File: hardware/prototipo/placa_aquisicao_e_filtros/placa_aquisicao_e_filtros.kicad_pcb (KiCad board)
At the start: 2 copper layers, 20 parts, among them J1 Conn_01x04, J2 Conn_02x04_Odd_Even, J3 Conn_01x02, U1 Opamp_Quad_Generic, U2 AD620

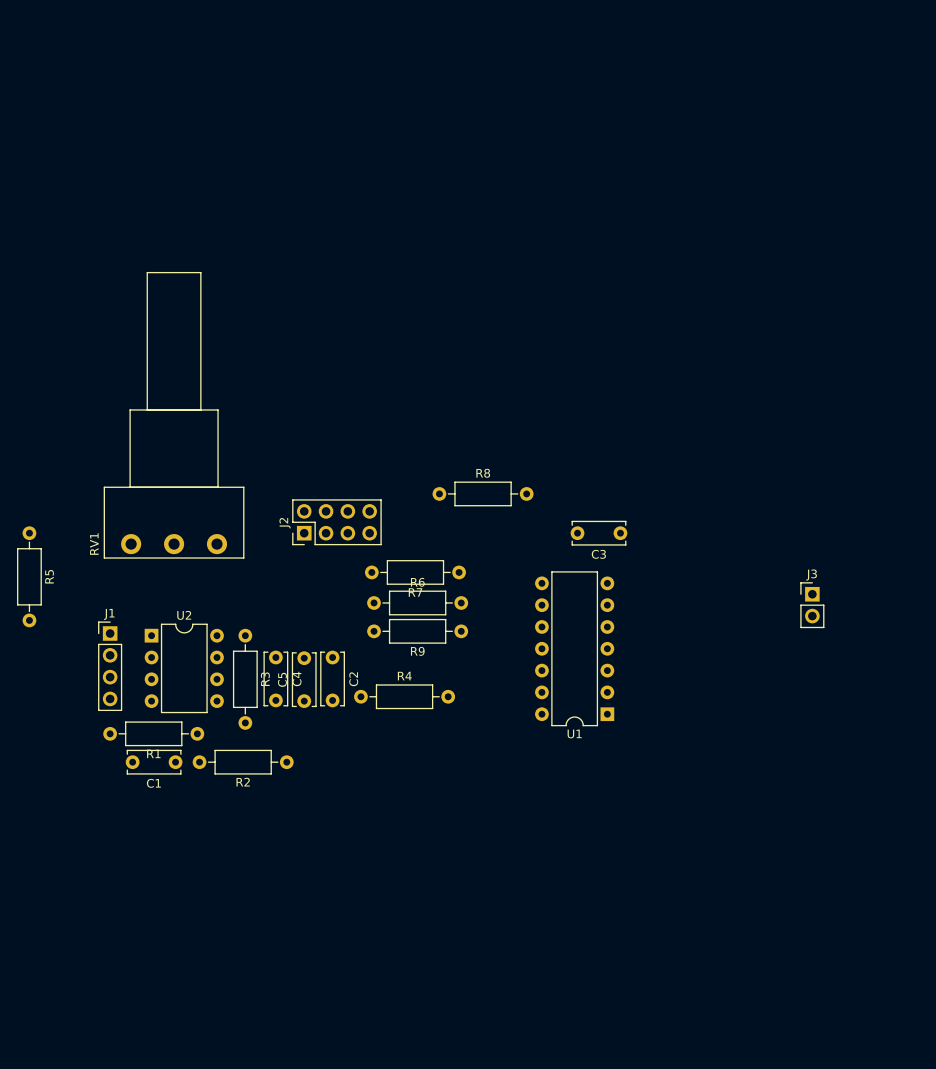
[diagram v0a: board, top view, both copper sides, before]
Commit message: Acquisition PCB prototype in development.
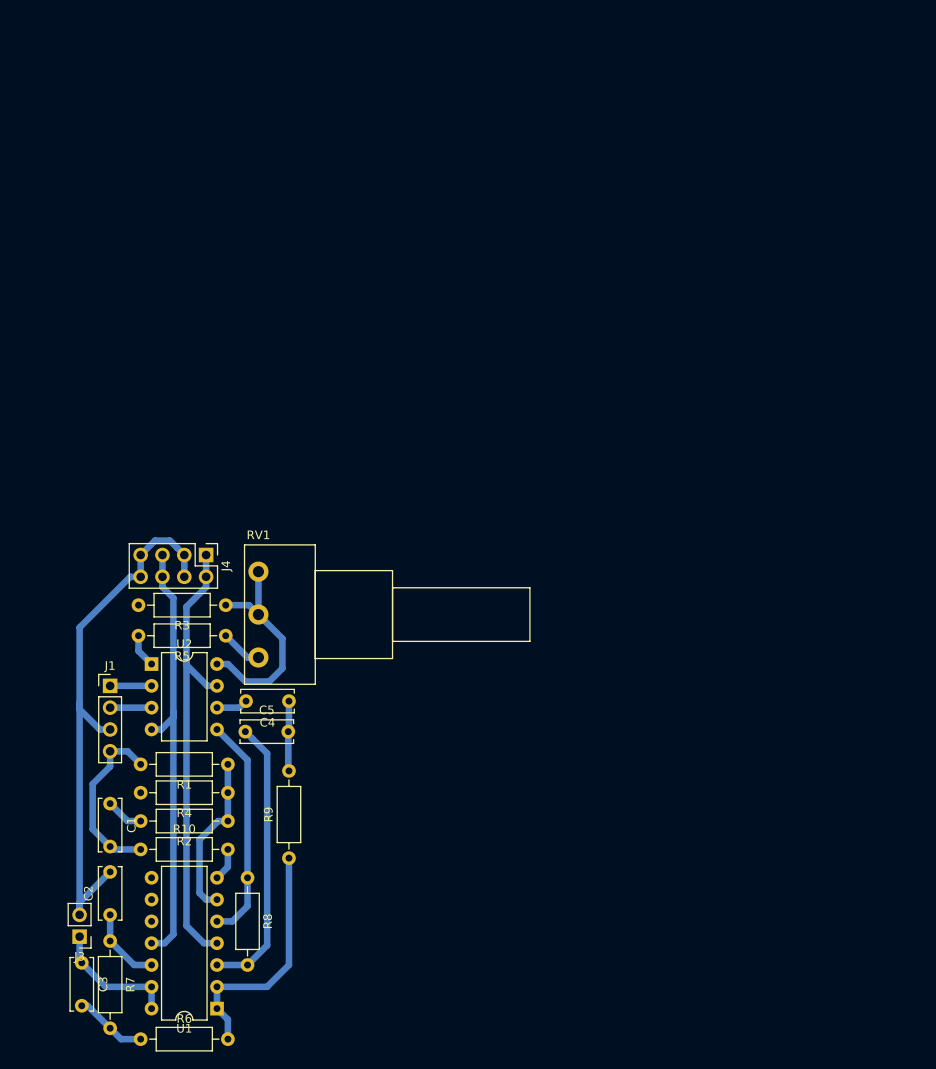
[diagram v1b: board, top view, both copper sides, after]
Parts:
- removed J2: Conn_02x04_Odd_Even, Connector_PinHeader_2.54mm:PinHeader_2x04_P2.54mm_Vertical
- added J4: Conn_02x04_Counter_Clockwise, Connector_PinHeader_2.54mm:PinHeader_2x04_P2.54mm_Vertical, F.Cu at (104.6, 83.6)
- added R10: 0R, Resistor_THT:R_Axial_DIN0207_L6.3mm_D2.5mm_P10.16mm_Horizontal, F.Cu at (97.0, 117.9)
- moved J3 94.2 mm to (89.9, 128.0), turned to 180 degrees
- moved C3 80.2 mm to (90.2, 131.1), turned to 270 degrees
- moved R7 59.1 mm to (93.5, 128.5), turned to 270 degrees
- moved R6 57.6 mm to (97.0, 140.0)
- moved U1 56.9 mm to (105.9, 136.4)
- moved R8 50.0 mm to (109.5, 121.2), turned to 270 degrees
- moved C2 39.6 mm to (93.5, 125.5), turned to 90 degrees
- moved R9 33.2 mm to (114.3, 118.9), turned to 90 degrees
- moved R5 25.8 mm to (106.9, 93.0), turned to 180 degrees
- moved R4 19.1 mm to (107.2, 111.3), turned to 180 degrees
- moved RV1 14.1 mm to (110.7, 95.5), turned to 0 degrees
- moved R2 9.70 mm to (107.2, 114.6)
- moved C1 9.02 mm to (93.5, 112.5), turned to 270 degrees
- moved C5 7.73 mm to (109.2, 104.1), turned to 0 degrees
- moved J1 6.10 mm to (93.5, 98.8)
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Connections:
- RV1 pad 1: Net-(R3-Pad1) -> Net-(R5-Pad1)
- RV1 pad 2: Net-(R5-Pad1) -> Net-(R3-Pad1)
- RV1 pad 3: Net-(R5-Pad1) -> Net-(R3-Pad1)
- U1 pad 1: ref_electrode -> out2
- U1 pad 10: Net-(C5-Pad1) -> (no net)
- U1 pad 11: (no net) -> -9V
- U1 pad 2: Net-(R1-Pad1) -> out2
- U1 pad 3: GNDA -> Net-(C5-Pad1)
- U1 pad 4: (no net) -> +9V
- U1 pad 5: Net-(C2-Pad1) -> GNDA
- U1 pad 6: out3 -> Net-(R1-Pad1)
- U1 pad 7: out3 -> Net-(R10-Pad2)
- U1 pad 8: out2 -> (no net)
- U1 pad 9: out2 -> (no net)
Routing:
- net GNDA: track 0.00 -> 92.6 mm
- net +9V: track 0.00 -> 53.7 mm
- net -9V: track 0.00 -> 51.4 mm
- net Net-(C5-Pad1): track 0.00 -> 32.7 mm
- net out2: track 0.00 -> 28.5 mm
- net Net-(R3-Pad1): track 0.00 -> 25.8 mm
- net ref_electrode: track 0.00 -> 20.7 mm
- net Net-(R1-Pad1): track 0.00 -> 19.4 mm
- net out3: track 0.00 -> 15.0 mm
- net Net-(C2-Pad1): track 0.00 -> 9.03 mm
- net Net-(C3-Pad2): track 0.00 -> 8.47 mm
- net Net-(C4-Pad1): track 0.00 -> 8.19 mm
- net Net-(R5-Pad1): track 0.00 -> 4.86 mm
- net right_electrode: track 0.00 -> 4.83 mm
- net left_electrode: track 0.00 -> 4.83 mm
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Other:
- net class Default: clearance 0.2 -> 0.45; trace_width 0.25 -> 0.762
- rule trace_clearance: 0.2 -> 0.45

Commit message: Acquisition prototype board finalized.
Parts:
- removed R10: 0R, Resistor_THT:R_Axial_DIN0207_L6.3mm_D2.5mm_P10.16mm_Horizontal
- added C6: 47u, Capacitors_THT:C_Disc_D6.0mm_W2.5mm_P5.00mm, F.Cu at (155.4, 107.8)
- added R11: 130k, Resistors_THT:R_Axial_DIN0207_L6.3mm_D2.5mm_P10.16mm_Horizontal, F.Cu at (153.8, 78.5)
- added R12: 18k, Resistors_THT:R_Axial_DIN0207_L6.3mm_D2.5mm_P10.16mm_Horizontal, F.Cu at (155.2, 122.0)
- R8: value 91k -> 33k
- R9: value 47k -> 150k
- moved R8 55.6 mm to (155.4, 89.9)
- moved C5 52.0 mm to (160.5, 95.5), turned to 90 degrees
- moved R9 50.4 mm to (160.4, 98.4), turned to 270 degrees
- moved J4 50.2 mm to (149.9, 61.7)
- moved R3 50.2 mm to (152.1, 67.6)
- moved RV1 50.2 mm to (156.0, 73.7)
- moved U2 50.2 mm to (143.5, 74.4)
- moved R5 50.2 mm to (152.1, 71.1)
- moved R1 49.3 mm to (152.4, 88.4)
- moved C4 48.6 mm to (159.1, 81.9)
- moved C1 48.2 mm to (138.7, 95.8)
- moved C2 48.2 mm to (138.7, 108.7)
- moved C3 48.2 mm to (135.4, 114.3)
- moved R2 48.2 mm to (152.4, 97.8)
- moved R4 48.2 mm to (152.4, 94.5)
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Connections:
- J1 pad 1: right_electrode -> left_electrode
- J1 pad 2: left_electrode -> right_electrode
- R8 pad 2: Net-(C5-Pad1) -> Net-(C4-Pad1)
- R9 pad 1: out2 -> Net-(C5-Pad1)
- R9 pad 2: Net-(C4-Pad1) -> out2
- U1 pad 2: out2 -> Net-(C5-Pad1)
- U1 pad 3: Net-(C5-Pad1) -> Net-(R11-Pad2)
- U1 pad 7: Net-(R10-Pad2) -> ref_electrode
- U2 pad 2: right_electrode -> left_electrode
- U2 pad 3: left_electrode -> right_electrode
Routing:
- net GNDA: track 92.6 -> 169.4 mm, vias 0 -> 4
- net Net-(R11-Pad2): track 0.00 -> 65.2 mm
- net Net-(R1-Pad1): track 19.4 -> 60.8 mm, vias 0 -> 4
- net Net-(R4-Pad2): track 3.93 -> 33.0 mm, vias 0 -> 2
- net ref_electrode: track 20.7 -> 44.0 mm, vias 0 -> 2
- net Net-(C4-Pad1): track 8.19 -> 25.0 mm
- net Net-(C5-Pad1): track 32.7 -> 48.8 mm
- net +9V: track 53.7 -> 61.5 mm
- net -9V: track 51.4 -> 55.9 mm
- net Net-(R10-Pad2): track 3.83 -> 0.00 mm
- net right_electrode: track 4.83 -> 8.38 mm
- net left_electrode: track 4.83 -> 8.38 mm
- net out2: track 28.5 -> 30.6 mm
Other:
- board outline added: 35.6 x 69.8 mm

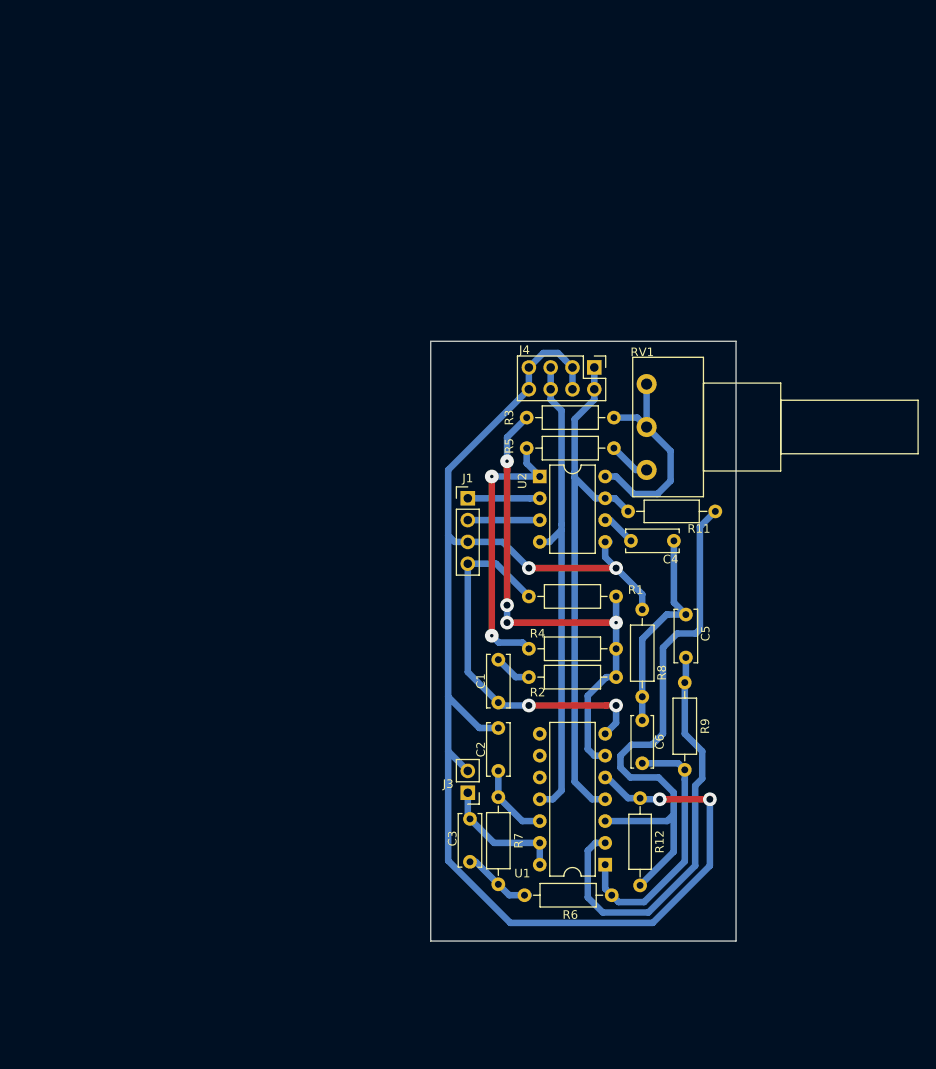
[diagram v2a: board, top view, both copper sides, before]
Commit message: PCB with AGC routed but negative supply without voltage regulator
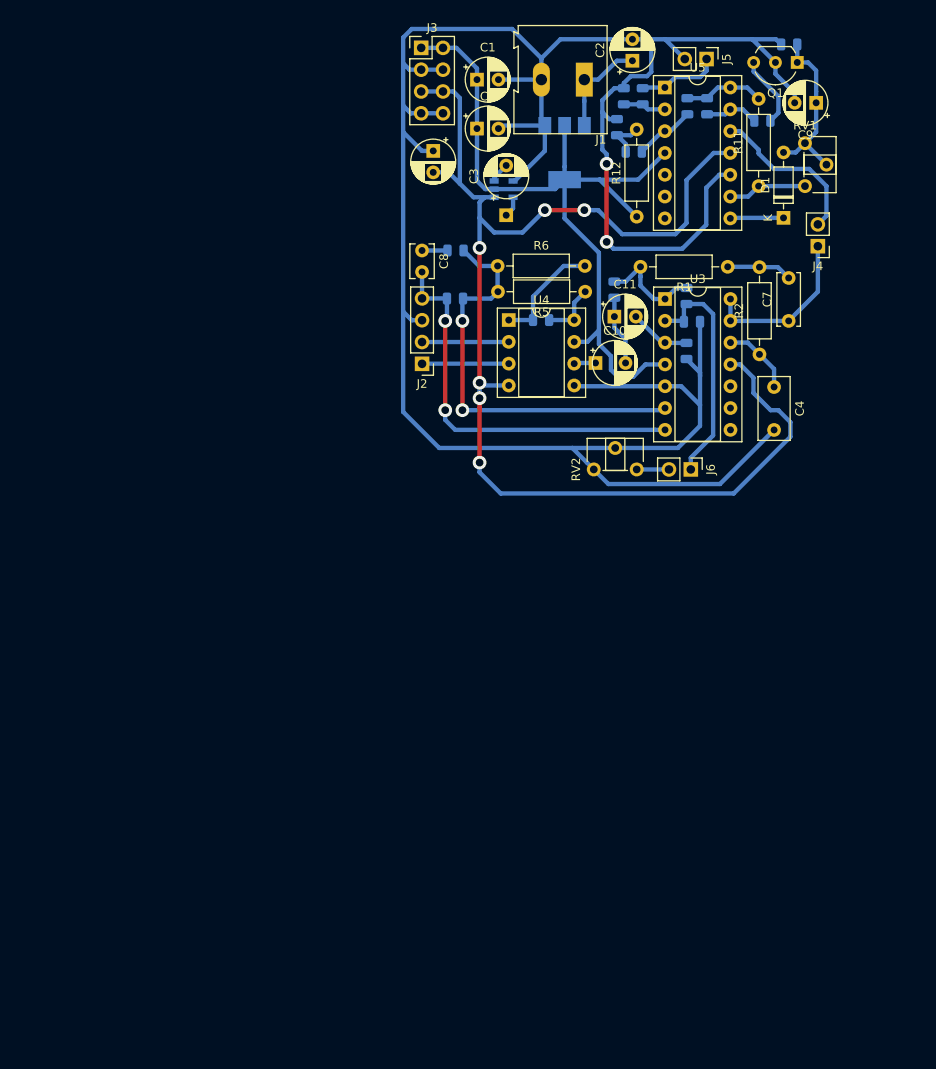
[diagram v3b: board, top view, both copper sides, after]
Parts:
- added C10: 47u, Capacitor_THT:CP_Radial_D5.0mm_P2.50mm, F.Cu at (151.0, 61.2)
- added C11: 47u, Capacitor_THT:CP_Radial_D5.0mm_P2.50mm, F.Cu at (152.2, 55.8)
- added C7: 100n, Capacitor_THT:C_Disc_D6.0mm_W2.5mm_P5.00mm, F.Cu at (172.5, 56.3)
- added C8: 100p, Capacitor_THT:C_Disc_D3.8mm_W2.6mm_P2.50mm, F.Cu at (129.8, 48.1)
- added C9: 22u, Capacitor_THT:CP_Radial_D5.0mm_P2.50mm, F.Cu at (175.7, 30.9)
- added D1: 1N4148, Diode_THT:D_DO-35_SOD27_P7.62mm_Horizontal, F.Cu at (171.9, 44.3)
- added J2: Conn_01x04, Connector_PinHeader_2.54mm:PinHeader_1x04_P2.54mm_Vertical, F.Cu at (129.8, 61.3)
- added J5: Conn_01x02, Connector_PinHeader_2.54mm:PinHeader_1x02_P2.54mm_Vertical, F.Cu at (162.9, 25.8)
- added J6: Conn_01x02, Connector_PinHeader_2.54mm:PinHeader_1x02_P2.54mm_Vertical, F.Cu at (161.1, 73.6)
- added Q1: BF245B, Package_TO_SOT_THT:TO-92_Inline_Wide, F.Cu at (173.5, 26.2)
- added R10: 100k, Resistor_SMD:R_0805_2012Metric, B.Cu at (172.6, 24.1)
- added R13: 22k, Resistor_SMD:R_0805_2012Metric, B.Cu at (152.5, 33.7)
- added R14: 1k, Resistor_SMD:R_0805_2012Metric, B.Cu at (160.7, 31.3)
- added R15: 1k, Resistor_SMD:R_0805_2012Metric, B.Cu at (154.5, 36.6)
- added R16: 47k, Resistor_SMD:R_0805_2012Metric, B.Cu at (160.6, 59.8)
- added R17: 12k, Resistor_SMD:R_0805_2012Metric, B.Cu at (153.3, 30.1)
- added R18: 12k, Resistor_SMD:R_0805_2012Metric, B.Cu at (155.5, 30.1)
- added R19: 100k, Resistor_SMD:R_0805_2012Metric, B.Cu at (152.2, 52.7)
- added R20: 68k, Resistor_SMD:R_0805_2012Metric, B.Cu at (161.2, 56.4)
- added R21: 150k, Resistor_SMD:R_0805_2012Metric, B.Cu at (160.6, 53.4)
- added RV2: R_POT, Potentiometer_THT:Potentiometer_ACP_CA6-H2,5_Horizontal, F.Cu at (149.8, 73.6)
- added U3: Opamp_Quad_Generic, Package_DIP:DIP-14_W7.62mm_Socket, F.Cu at (158.1, 53.8)
- added U4: AD620, Package_DIP:DIP-8_W7.62mm_Socket, F.Cu at (139.9, 56.2)
- added U5: Opamp_Quad_Generic, Package_DIP:DIP-14_W7.62mm_Socket, F.Cu at (158.1, 29.1)
- C1: value 100p -> 1u; footprint Capacitor_THT:C_Disc_D6.0mm_W2.5mm_P5.00mm -> Capacitor_THT:CP_Radial_D5.0mm_P2.50mm
- C2: value 47n -> 10u; footprint Capacitor_THT:C_Disc_D6.0mm_W2.5mm_P5.00mm -> Capacitor_THT:CP_Radial_D5.0mm_P2.50mm
- C3: value 100n -> 1u; footprint Capacitor_THT:C_Disc_D6.0mm_W2.5mm_P5.00mm -> Capacitor_THT:CP_Radial_D5.0mm_P2.50mm
- C4: value 47u -> 47n; footprint Capacitor_THT:C_Disc_D6.0mm_W2.5mm_P5.00mm -> Capacitor_THT:C_Rect_L7.2mm_W3.5mm_P5.00mm_FKS2_FKP2_MKS2_MKP2
- C5: value 47u -> 10u; footprint Capacitor_THT:C_Disc_D6.0mm_W2.5mm_P5.00mm -> Capacitor_THT:CP_Radial_D5.0mm_P2.50mm
- C6: value 47u -> 1u; footprint Capacitors_THT:C_Disc_D6.0mm_W2.5mm_P5.00mm -> Capacitor_THT:CP_Radial_D5.0mm_P2.50mm
- J1: value Conn_01x04 -> Conn_01x02; footprint Connector_PinHeader_2.54mm:PinHeader_1x04_P2.54mm_Vertical -> TerminalBlock:TerminalBlock_Altech_AK300-2_P5.00mm
- J3: value Conn_01x02 -> Conn_02x04_Counter_Clockwise; footprint Connector_PinHeader_2.54mm:PinHeader_1x02_P2.54mm_Vertical -> Connector_PinHeader_2.54mm:PinHeader_2x04_P2.54mm_Vertical
- J4: value Conn_02x04_Counter_Clockwise -> Conn_01x02; footprint Connector_PinHeader_2.54mm:PinHeader_2x04_P2.54mm_Vertical -> Connector_PinHeader_2.54mm:PinHeader_1x02_P2.54mm_Vertical
- R1: value 1M -> 18k
- R11: value 130k -> 200k; footprint Resistors_THT:R_Axial_DIN0207_L6.3mm_D2.5mm_P10.16mm_Horizontal -> Resistor_THT:R_Axial_DIN0207_L6.3mm_D2.5mm_P10.16mm_Horizontal
- R12: value 18k -> 51k; footprint Resistors_THT:R_Axial_DIN0207_L6.3mm_D2.5mm_P10.16mm_Horizontal -> Resistor_THT:R_Axial_DIN0207_L6.3mm_D2.5mm_P10.16mm_Horizontal
- R2: value 10k -> 30k
- R3: value 24.9k -> 1M; footprint Resistor_THT:R_Axial_DIN0207_L6.3mm_D2.5mm_P10.16mm_Horizontal -> Resistor_SMD:R_0805_2012Metric; moved to B.Cu
- R4: value 24.9k -> 12k; footprint Resistor_THT:R_Axial_DIN0207_L6.3mm_D2.5mm_P10.16mm_Horizontal -> Resistor_SMD:R_0805_2012Metric; moved to B.Cu
- R5: value 75R -> 24k
- R6: value 18k -> 24k
- R7: value 30k -> 560R; footprint Resistor_THT:R_Axial_DIN0207_L6.3mm_D2.5mm_P10.16mm_Horizontal -> Resistor_SMD:R_0805_2012Metric; moved to B.Cu
- R8: value 33k -> 12k; footprint Resistor_THT:R_Axial_DIN0207_L6.3mm_D2.5mm_P10.16mm_Horizontal -> Resistor_SMD:R_0805_2012Metric; moved to B.Cu
- R9: value 150k -> 75R; footprint Resistor_THT:R_Axial_DIN0207_L6.3mm_D2.5mm_P10.16mm_Horizontal -> Resistor_SMD:R_0805_2012Metric; moved to B.Cu
- RV1: value 1k -> 470k; footprint Potentiometer_THT:Potentiometer_Piher_PC-16_Single_Horizontal -> Potentiometer_THT:Potentiometer_ACP_CA6-H2,5_Horizontal
- U1: value Opamp_Quad_Generic -> AP1117-33; footprint Package_DIP:DIP-14_W7.62mm -> Package_TO_SOT_SMD:SOT-223-3_TabPin2; moved to B.Cu
- U2: value AD620 -> TPS60401; footprint Package_DIP:DIP-8_W7.62mm -> Package_TO_SOT_SMD:SOT-23-5; moved to B.Cu
- moved J3 86.9 mm to (129.7, 24.5), turned to 0 degrees
- moved R7 84.6 mm to (169.4, 33.0), turned to 0 degrees
- moved C2 84.2 mm to (154.3, 26.0)
- moved U1 83.1 mm to (146.4, 36.7), turned to 270 degrees
- moved R12 77.9 mm to (154.8, 44.2)
- moved C6 75.4 mm to (131.1, 36.5), turned to 270 degrees
- moved C3 73.7 mm to (139.6, 40.7), turned to 90 degrees
- moved R6 73.4 mm to (138.6, 49.9)
- moved C1 67.6 mm to (136.2, 28.2), turned to 0 degrees
- moved C5 66.2 mm to (136.2, 33.9), turned to 0 degrees
- moved R8 59.1 mm to (163.0, 31.3)
- moved J1 50.6 mm to (148.7, 28.2), turned to 180 degrees
- moved R4 50.0 mm to (133.7, 48.1)
- moved R9 45.4 mm to (143.7, 56.2), turned to 180 degrees
- moved RV1 42.3 mm to (174.4, 35.6)
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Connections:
- C1 pad 1: Net-(C1-Pad1) -> +3V3
- C1 pad 2: ref_electrode -> GNDA
- C2 pad 1: Net-(C2-Pad1) -> +Vin
- C3 pad 1: out3 -> Net-(C3-Pad1)
- C4 pad 2: out1 -> GNDA
- C5 pad 1: Net-(C5-Pad1) -> +3V3
- C5 pad 2: Net-(C4-Pad1) -> GNDA
- C6 pad 1: out2 -> GNDA
- C6 pad 2: Net-(C4-Pad1) -> -3V3
- J1 pad 1: left_electrode -> +Vin
- J1 pad 2: right_electrode -> GNDA
- J3 pad 1: out3 -> +3V3
- J3 pad 2: GNDA -> +3V3
- J4 pad 1: +9V -> AGC
- J4 pad 2: +9V -> Net-(J4-Pad2)
- R1 pad 1: Net-(R1-Pad1) -> Net-(C7-Pad2)
- R1 pad 2: ref_electrode -> LP
- R11 pad 1: +9V -> Net-(R11-Pad1)
- R11 pad 2: Net-(R11-Pad2) -> SUM
- R12 pad 1: Net-(R11-Pad2) -> +3V3
- R12 pad 2: GNDA -> Net-(R12-Pad2)
- R2 pad 1: Net-(R1-Pad1) -> Net-(C4-Pad1)
- R2 pad 2: Net-(C1-Pad1) -> Net-(C7-Pad2)
- R3 pad 2: Net-(R1-Pad1) -> ref_electrode
- R4 pad 1: Net-(R1-Pad1) -> Net-(R3-Pad1)
- R4 pad 2: Net-(R4-Pad2) -> Net-(C8-Pad1)
- R5 pad 2: Net-(R4-Pad2) -> Net-(R3-Pad1)
- R6 pad 1: Net-(C3-Pad2) -> Net-(R3-Pad1)
- R6 pad 2: out2 -> Net-(R6-Pad2)
- R7 pad 1: Net-(C2-Pad1) -> Net-(R7-Pad1)
- R7 pad 2: Net-(C3-Pad2) -> Net-(Q1-Pad3)
- R8 pad 1: GNDA -> SUM
- R8 pad 2: Net-(C4-Pad1) -> Net-(R7-Pad1)
- R9 pad 1: Net-(C5-Pad1) -> Net-(R5-Pad1)
- R9 pad 2: out2 -> Net-(R6-Pad2)
- RV1 pad 1: Net-(R5-Pad1) -> Net-(C9-Pad1)
- RV1 pad 2: Net-(R3-Pad1) -> Net-(C9-Pad1)
- RV1 pad 3: Net-(R3-Pad1) -> Net-(R11-Pad1)
- U1 pad 1: out2 -> GNDA
- U1 pad 2: Net-(C5-Pad1) -> +3V3
- U1 pad 3: Net-(R11-Pad2) -> +Vin
- U2 pad 1: Net-(R4-Pad2) -> -3V3
- U2 pad 2: left_electrode -> +3V3
- U2 pad 3: right_electrode -> Net-(C3-Pad2)
- U2 pad 4: -9V -> GNDA
- U2 pad 5: GNDA -> Net-(C3-Pad1)
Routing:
- net -3V3: track 0.00 -> 150.4 mm, vias 0 -> 6
- net GNDA: track 169.4 -> 294.7 mm, vias 4 -> 2
- net +3V3: track 0.00 -> 92.0 mm
- net Net-(R11-Pad2): track 65.2 -> 0.00 mm
- net +9V: track 61.5 -> 0.00 mm
- net Net-(R1-Pad1): track 60.8 -> 0.00 mm, vias 4 -> 0
- net -9V: track 55.9 -> 0.00 mm
- net Net-(C5-Pad1): track 48.8 -> 0.00 mm
- net Net-(R4-Pad2): track 33.0 -> 0.00 mm, vias 2 -> 0
- net out2: track 30.6 -> 0.00 mm
- net Net-(J6-Pad1): track 0.00 -> 27.2 mm
- net Net-(R3-Pad1): track 25.8 -> 49.1 mm, vias 0 -> 2
- net Net-(C9-Pad1): track 0.00 -> 20.2 mm
- net AGC: track 0.00 -> 19.4 mm
- net Net-(J4-Pad2): track 0.00 -> 19.0 mm
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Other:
- board outline removed
- net class Default: clearance 0.45 -> 0.3048; trace_width 0.762 -> 0.508
- rule trace_clearance: 0.45 -> 0.3048
